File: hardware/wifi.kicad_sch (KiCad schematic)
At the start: 31 parts, among them J7 RJ45_Hanrun_HR913550A_Horizon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, U22 AP6212, Y2 26MHz

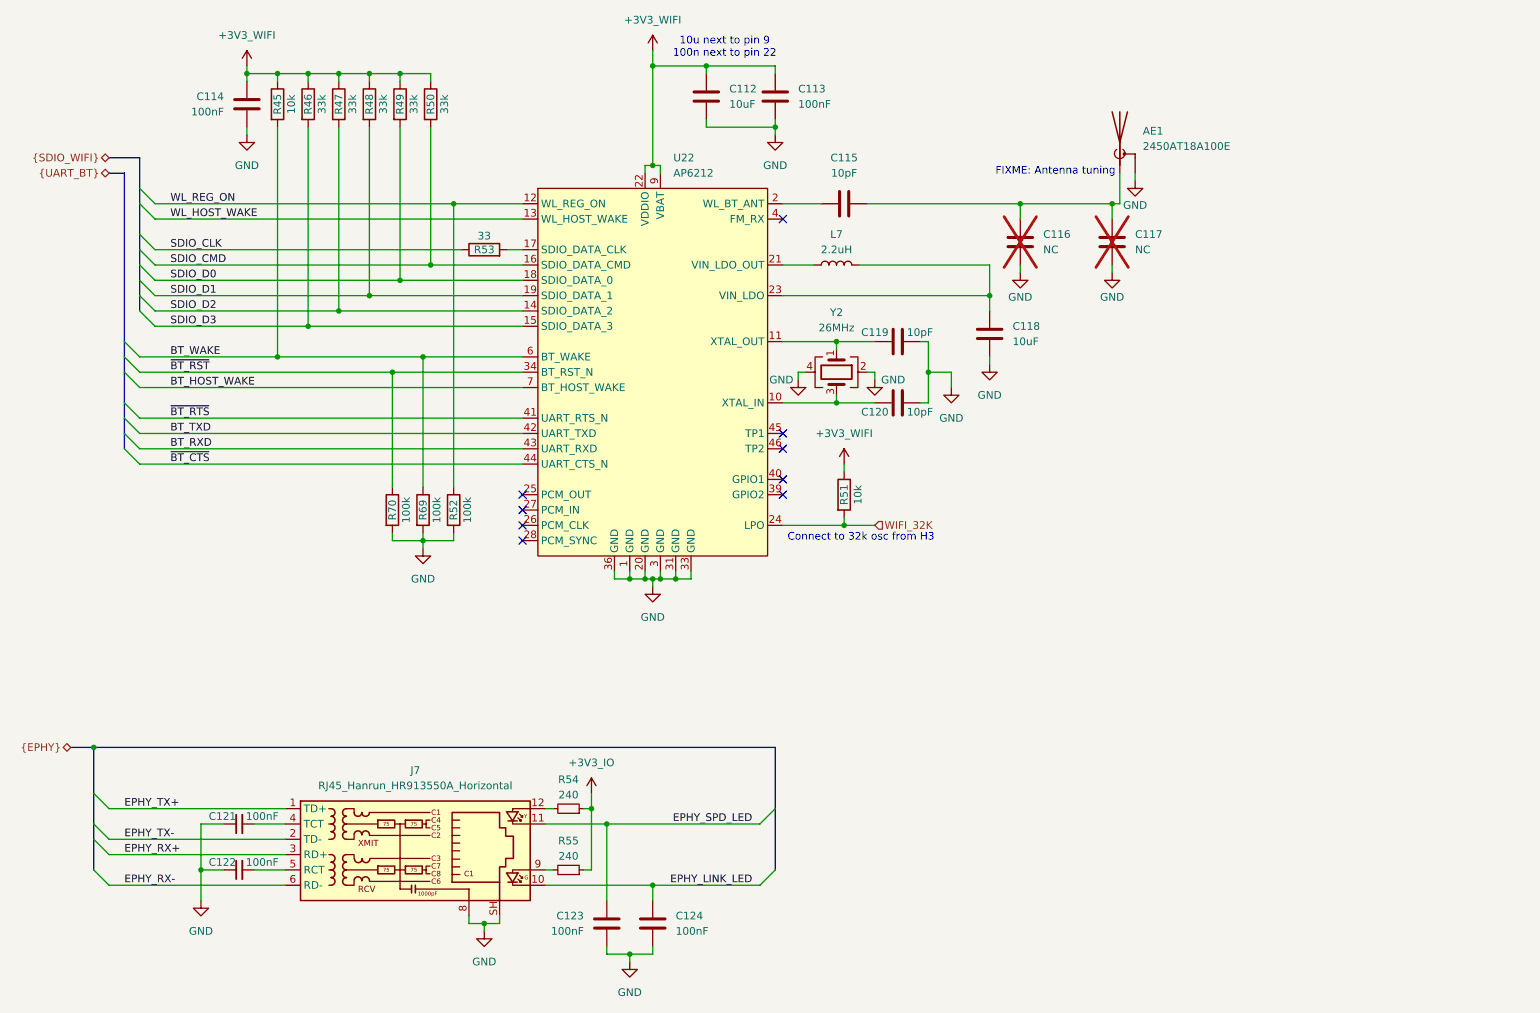
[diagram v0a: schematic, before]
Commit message: Less than 100 traces left
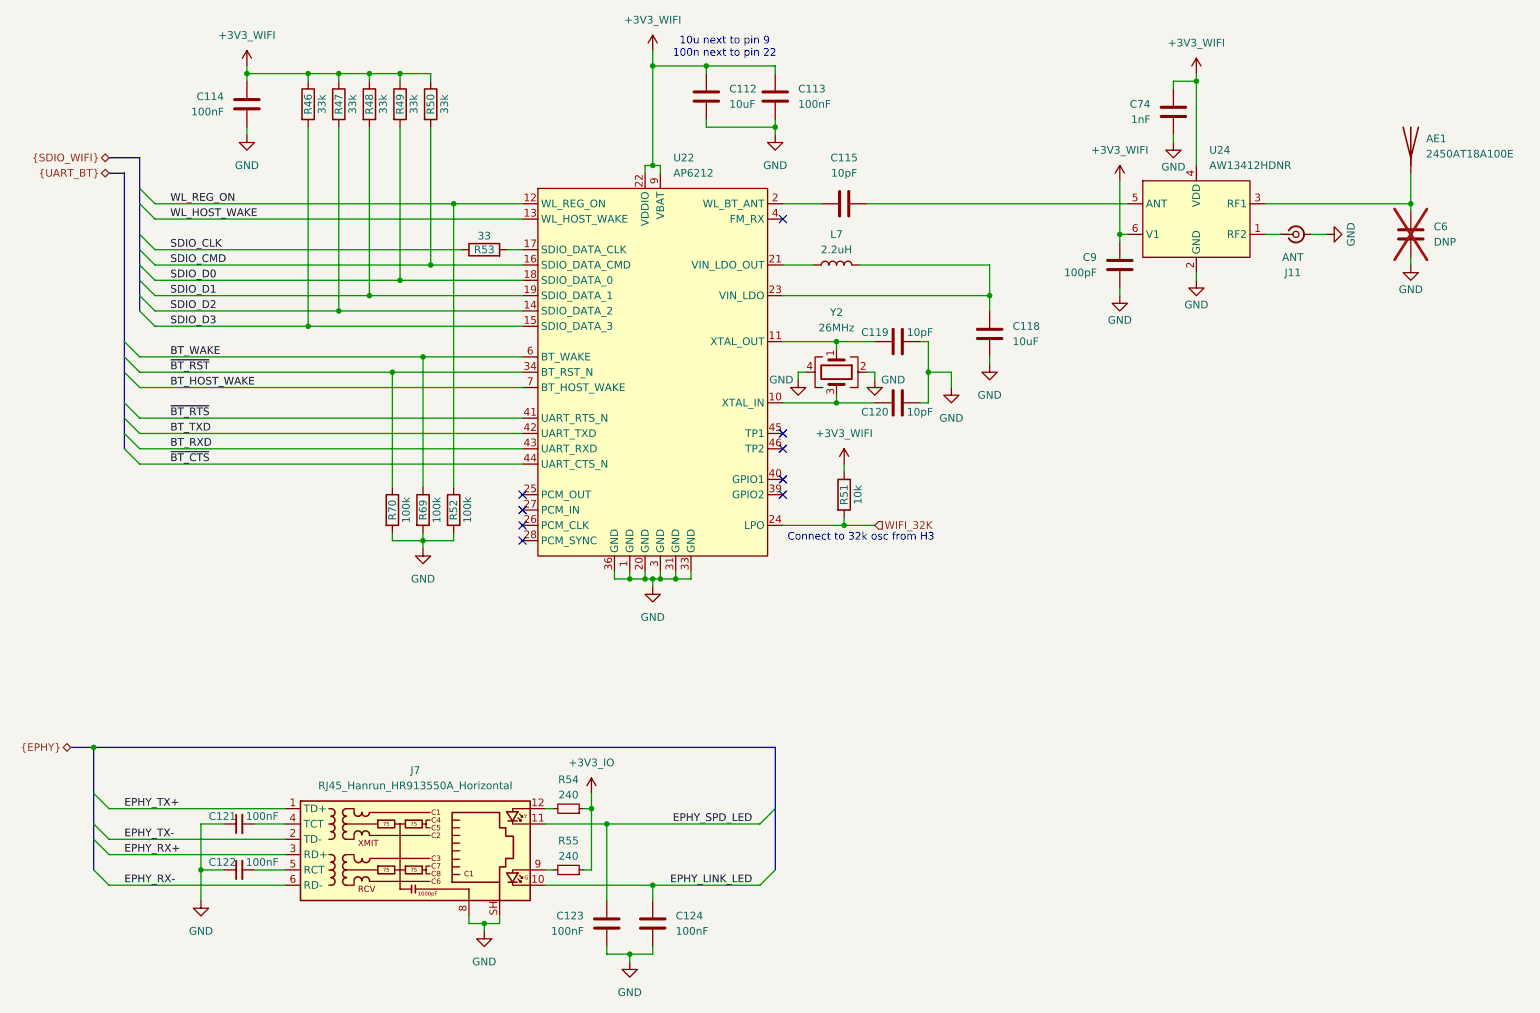
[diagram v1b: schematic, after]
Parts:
- removed C116, C117: NC, Capacitor_SMD:C_0402_1005Metric, symbol Device:C
- removed R45: 10k, Resistor_SMD:R_0402_1005Metric, symbol Device:R
- added C6: DNP, symbol Device:C
- added C74: 1nF, Capacitor_SMD:C_0402_1005Metric, symbol Device:C
- added C9: 100pF, Capacitor_SMD:C_0402_1005Metric, symbol Device:C
- added J11: ANT, Connector_Coaxial:U.FL_Molex_MCRF_73412-0110_Vertical, symbol Connector:Conn_Coaxial_Small
- added U24: AW13412HDNR, cm0:DFN-6_1.1x0.7mm_P0.4mm, symbol cm0:AW13412HDNR
- AE1: symbol Device:Antenna_Shield -> Device:Antenna
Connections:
- net +3V3_WIFI: now also C74.1, C9.1, U24.4 (VDD), U24.6 (V1)
- net GND: now also C6.2, C74.2, C9.2, J11.2 (Ext), U24.2 (GND); no longer AE1.2 (Shield)
- net at AE1.1 (A): now also C6.1, U24.3 (RF1); no longer C115.2
- new net: J11.1 (In), U24.1 (RF2)
- new net: C115.2, U24.5 (ANT)
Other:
- note removed: "FIXME: Antenna tuning"
